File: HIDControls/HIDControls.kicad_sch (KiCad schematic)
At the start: 70 parts, among them M1 ModulePlug, M10 ModulePlug, M11 ModulePlug, M12 ModulePlug, M2 ModulePlug, M3 ModulePlug, M4 ModulePlug, M5 ModulePlug, M6 ModulePlug, M7 ModulePlug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

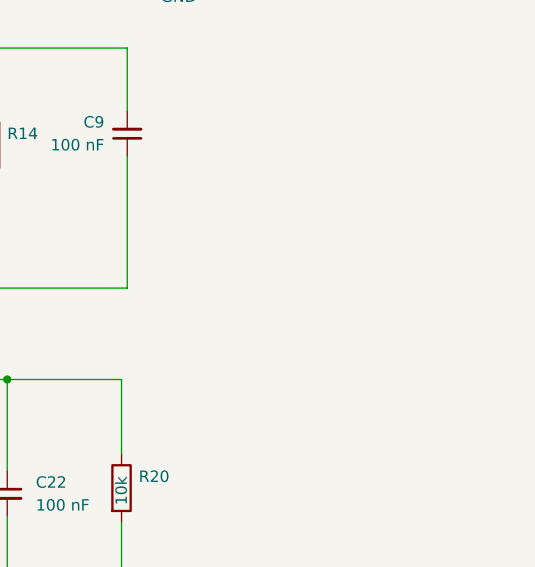
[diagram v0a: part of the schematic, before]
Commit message: Added AnalogJoystick
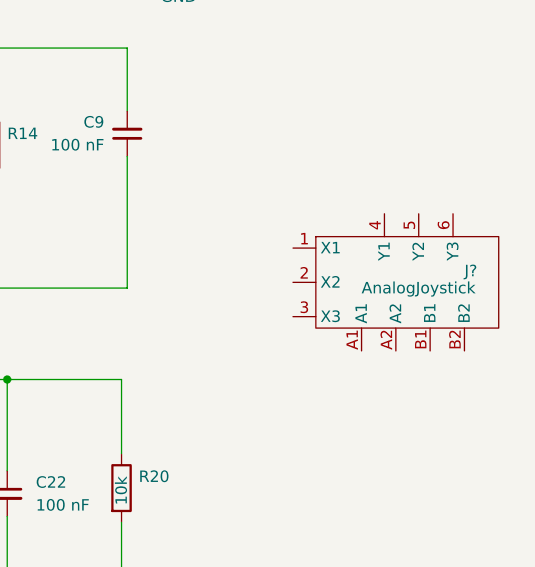
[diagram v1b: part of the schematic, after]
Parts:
- added J?: AnalogJoystick, HIDPanel:AnalogJoystick, symbol AnalogJoystick:AnalogJoystick
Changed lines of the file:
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@@
     (pin "3")
+  )
+  (symbol (lib_id "AnalogJoystick:AnalogJoystick") (at 263.525 90.805 0) (unit 1)
+    (in_bom yes) (on_board yes)
+    (property "Reference" "J?" (id 0) (at 268.605 89.535 0)
+      (effects (font (size 1.27 1.27)) (justify left))
+    )
+    (property "Value" "AnalogJoystick" (id 1) (at 257.175 91.44 0)
+      (effects (font (size 1.27 1.27)) (justify left))
+    )
+    (property "Footprint" "HIDPanel:AnalogJoystick" (id 2) (at 263.525 90.805 0)
+      (effects (font (size 1.27 1.27)) hide)
+    )
+    (property "Datasheet" "" (id 3) (at 263.525 90.805 0)
+      (effects (font (size 1.27 1.27)) hide)
+    )
+    (pin "1")
+    (pin "2")
+    (pin "3")
+    (pin "4")
+    (pin "5")
+    (pin "6")
+    (pin "A1")
+    (pin "A2")
+    (pin "B1")
+    (pin "B2")
   )
   (symbol (lib_id "Device:C_Small") (at 128.905 45.085 0) (mirror x) (unit 1)
@@
       (reference "C22") (unit 1) (value "100 nF") (footprint "Capacitor_THT:C_Disc_D5.0mm_W2.5mm_P2.50mm")
     )
+    (path "/3adf741e-ee3b-4a1a-a881-7c6033fd5bf2"
+      (reference "J?") (unit 1) (value "AnalogJoystick") (footprint "HIDPanel:AnalogJoystick")
+    )
     (path "/1ec98f11-002b-4940-a7f4-63f9c2c7b185"

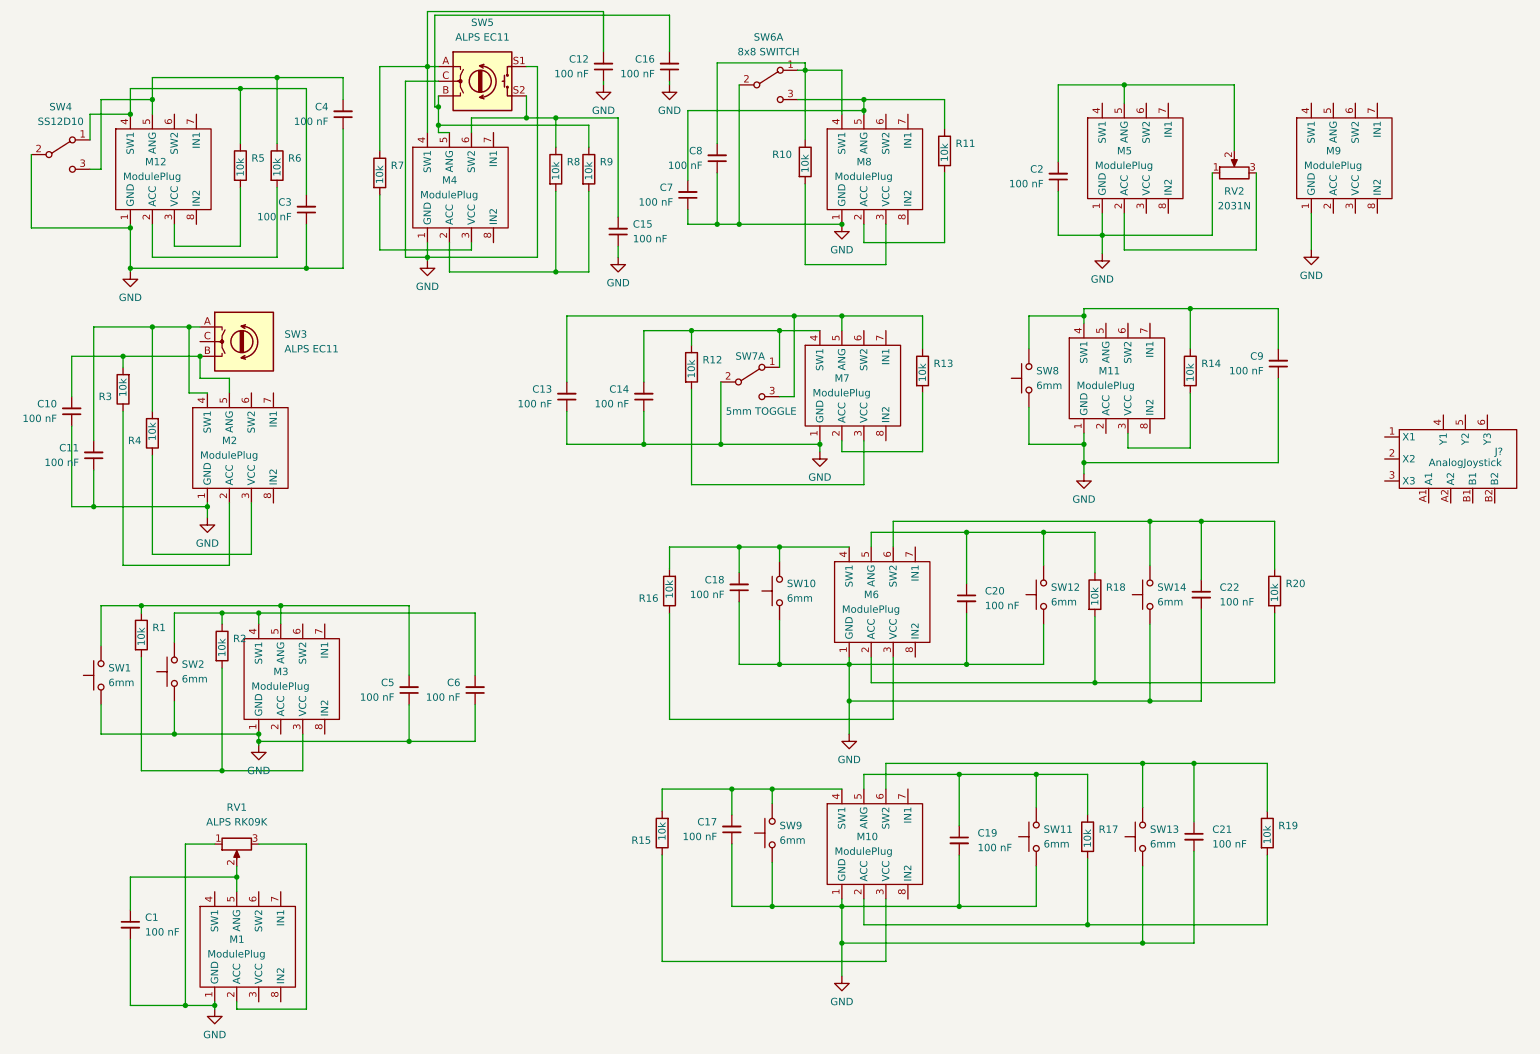
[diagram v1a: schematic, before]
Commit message: Added analog joystick device
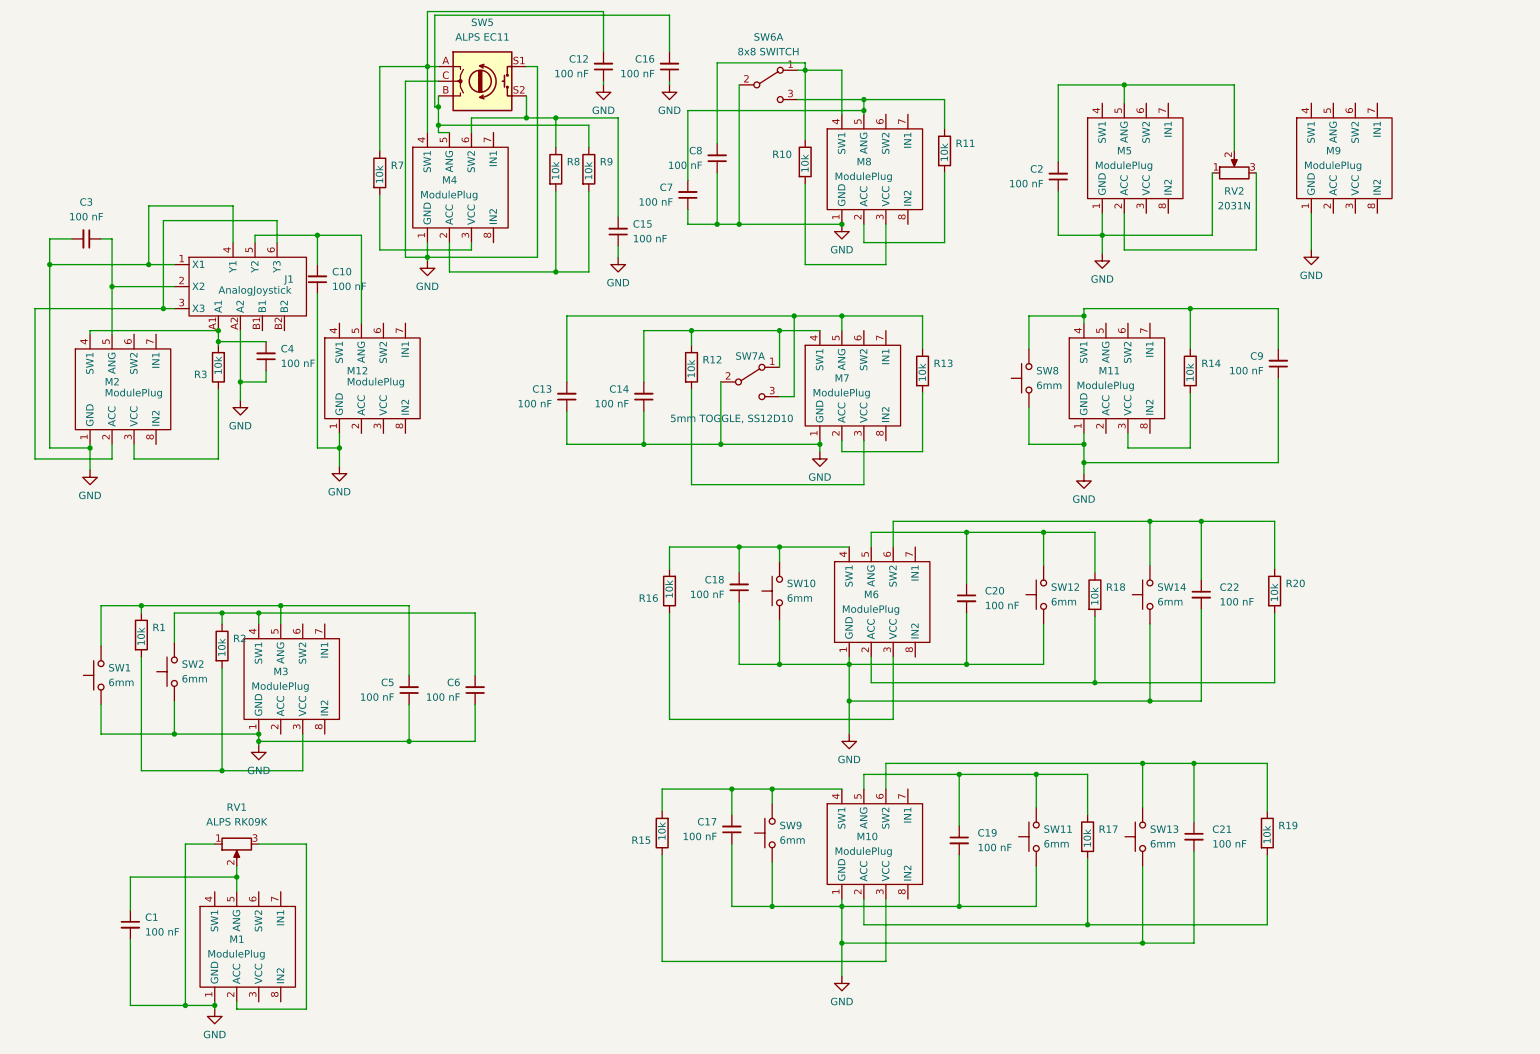
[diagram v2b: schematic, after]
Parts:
- removed C11: 100 nF, Capacitor_THT:C_Disc_D5.0mm_W2.5mm_P2.50mm, symbol Device:C_Small
- removed R4, R5, R6: 10k, Resistor_THT:R_Axial_DIN0207_L6.3mm_D2.5mm_P7.62mm_Horizontal, symbol Device:R
- removed SW3: ALPS EC11, Rotary_Encoder:RotaryEncoder_Alps_EC11E_Vertical_H20mm, symbol Device:RotaryEncoder
- removed SW4: SS12D10, HIDPanel:SS12D10, symbol Switch:SW_SPDT
- J1: renamed from J?; footprint HIDPanel:AnalogJoystick -> HIDControls:AnalogJoystick
- M10, M12: footprint HIDControls:ModulePlug -> HIDControls:RightPartModulePlug
- M2, M6: footprint HIDControls:ModulePlug -> HIDControls:LeftPartModulePlug
- SW7: value 5mm TOGGLE -> 5mm TOGGLE, SS12D10
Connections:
- net GND: now also C3.2, J1.1 (X1), J1.4 (Y1), J1.A2; no longer C3.1
- net at M12.4 (SW1): no longer C3.2
- net at C4.2: now also J1.A1, M2.4 (SW1), R3.2; no longer M12.5 (ANG)
- net at J1.2 (X2): now also C3.1, M2.5 (ANG)
- net at J1.3 (X3): now also J1.6 (Y3), M2.2 (ACC)
- net at J1.5 (Y2): now also C10.2, M12.5 (ANG)
- net at R3.1: now also M2.3 (VCC); no longer M2.2 (ACC)
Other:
- moved on the sheet: J1

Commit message: Added CAD models
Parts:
- M5: footprint HIDControls:ModulePlug -> HIDControls:LeftPartModulePlug
- M9: footprint HIDControls:ModulePlug -> HIDControls:RightPartModulePlug
- RV2: footprint HIDPanel:Linear-Pot-2031N -> HIDControls:Linear-Pot-2031N
- SW7: footprint HIDPanel:5mmSPDTtoggle -> HIDControls:5mmSPDTtoggle
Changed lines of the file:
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@@
     (property "Reference" "SW7" (id 0) (at 139.7 73.025 0))
     (property "Value" "5mm TOGGLE, SS12D10" (id 1) (at 136.525 83.82 0))
-    (property "Footprint" "HIDPanel:5mmSPDTtoggle" (id 2) (at 139.7 77.47 0)
+    (property "Footprint" "HIDControls:5mmSPDTtoggle" (id 2) (at 139.7 77.47 0)
       (effects (font (size 1.27 1.27)) hide)
     )
@@
     (property "Reference" "RV2" (id 0) (at 223.52 44.45 90))
     (property "Value" "2031N " (id 1) (at 223.52 46.99 90))
-    (property "Footprint" "HIDPanel:Linear-Pot-2031N" (id 2) (at 223.52 41.275 0)
+    (property "Footprint" "HIDControls:Linear-Pot-2031N" (id 2) (at 223.52 41.275 0)
       (effects (font (size 1.27 1.27)) hide)
     )
@@
       (effects (font (size 1.27 1.27)) (justify left))
     )
-    (property "Footprint" "HIDControls:ModulePlug" (id 2) (at 231.14 40.005 0)
+    (property "Footprint" "HIDControls:RightPartModulePlug" (id 2) (at 231.14 40.005 0)
       (effects (font (size 1.27 1.27)) (justify left) hide)
     )
@@
       (effects (font (size 1.27 1.27)) (justify left))
     )
-    (property "Footprint" "HIDControls:ModulePlug" (id 2) (at 194.945 40.005 0)
+    (property "Footprint" "HIDControls:LeftPartModulePlug" (id 2) (at 194.945 40.005 0)
       (effects (font (size 1.27 1.27)) (justify left) hide)
     )
@@
     )
     (path "/bb26dc0c-e42d-4466-bf87-a95a89397101"
-      (reference "M5") (unit 1) (value "ModulePlug") (footprint "HIDControls:ModulePlug")
+      (reference "M5") (unit 1) (value "ModulePlug") (footprint "HIDControls:LeftPartModulePlug")
     )
     (path "/83566ca3-f2cf-419f-8de8-edda09e8b966"
@@
     )
     (path "/a582a128-beec-4f1f-9d82-230c8222ebe1"
-      (reference "M9") (unit 1) (value "ModulePlug") (footprint "HIDControls:ModulePlug")
+      (reference "M9") (unit 1) (value "ModulePlug") (footprint "HIDControls:RightPartModulePlug")
     )
     (path "/153288e1-d413-4039-97de-f13133a8ef12"
@@
     )
     (path "/8233abc8-91d0-43e0-b3ff-321da3b974bd"
-      (reference "RV2") (unit 1) (value "2031N ") (footprint "HIDPanel:Linear-Pot-2031N")
+      (reference "RV2") (unit 1) (value "2031N ") (footprint "HIDControls:Linear-Pot-2031N")
     )
     (path "/2428a1f9-a856-4a72-972a-bff0d28ccc1d"
@@
     )
     (path "/7a7e8d1b-4780-4069-919b-789967f22157"
-      (reference "SW7") (unit 1) (value "5mm TOGGLE, SS12D10") (footprint "HIDPanel:5mmSPDTtoggle")
+      (reference "SW7") (unit 1) (value "5mm TOGGLE, SS12D10") (footprint "HIDControls:5mmSPDTtoggle")
     )
     (path "/ccfeeeb9-6e7b-4fe7-8b18-73c721a9e5c9"
